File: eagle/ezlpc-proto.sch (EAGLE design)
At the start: 61 parts, among them J1 MICRO USB, Q1 12Mhz, T1 MMBT3906, U1 PRTR5V0U2X, U2 MIC5225-3.3v, U3 LPC11U35FHI33/501, U4 BAS40-05

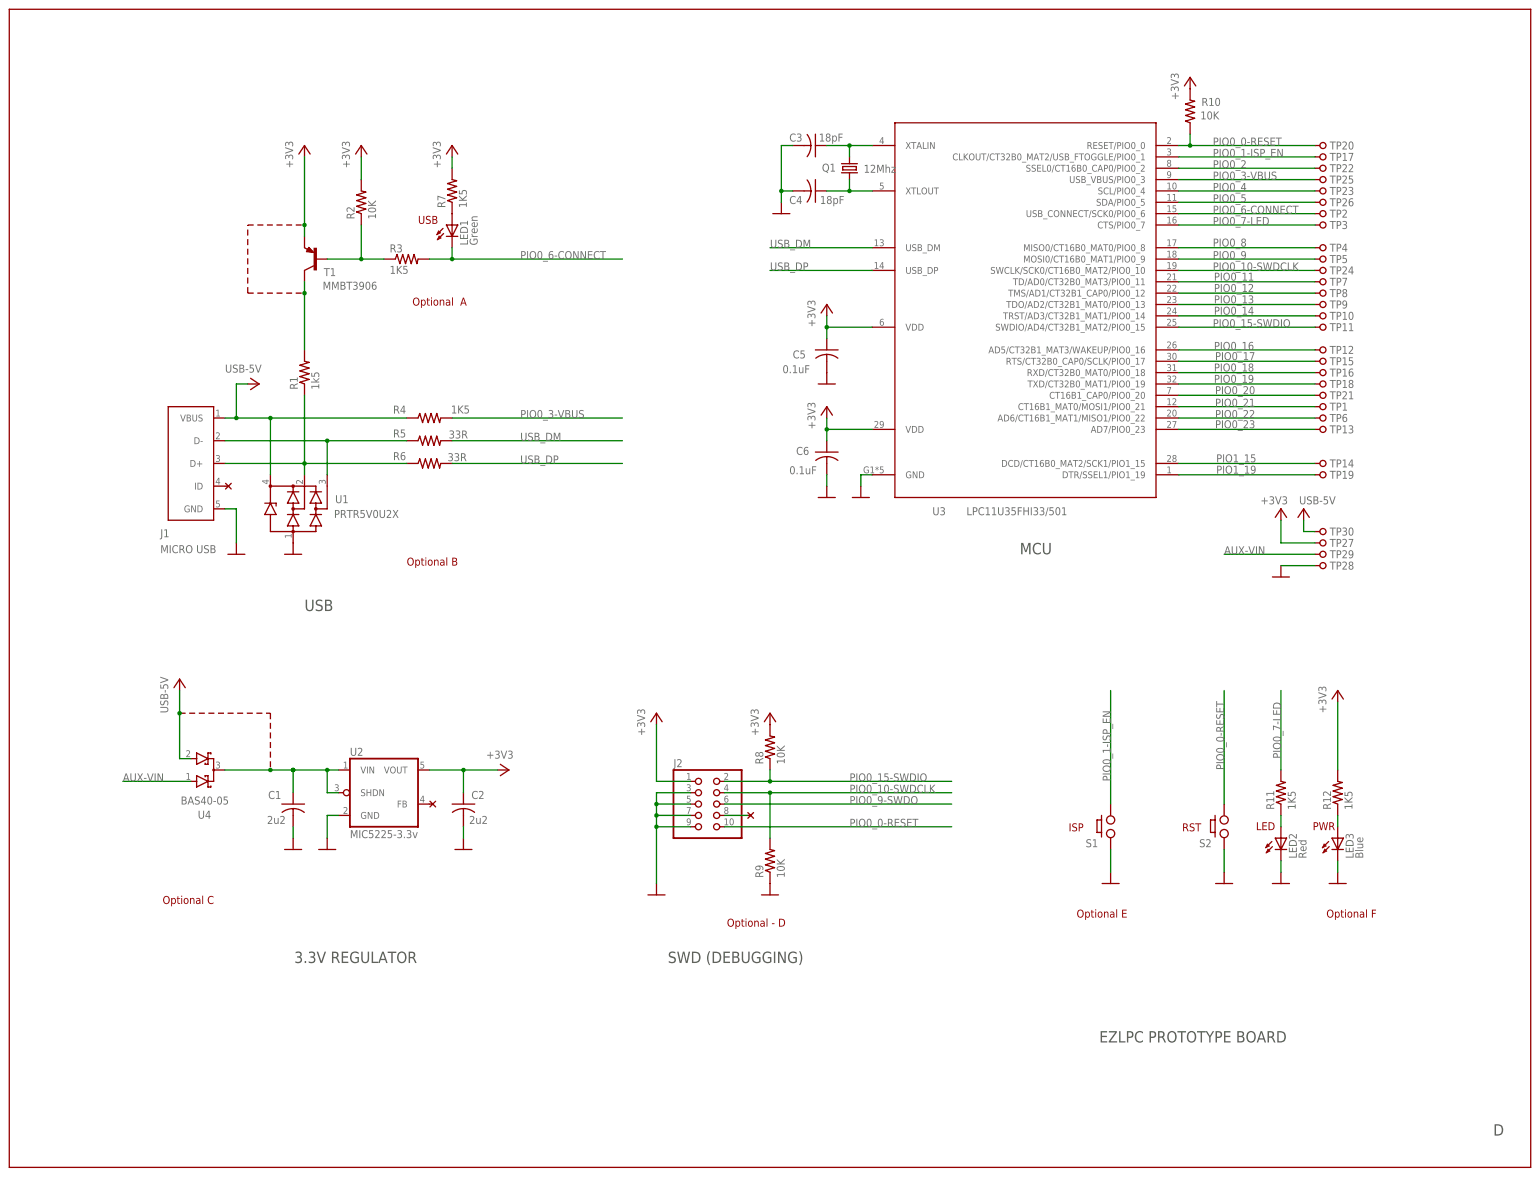
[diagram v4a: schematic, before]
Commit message: Cleaned up ERC warnings.
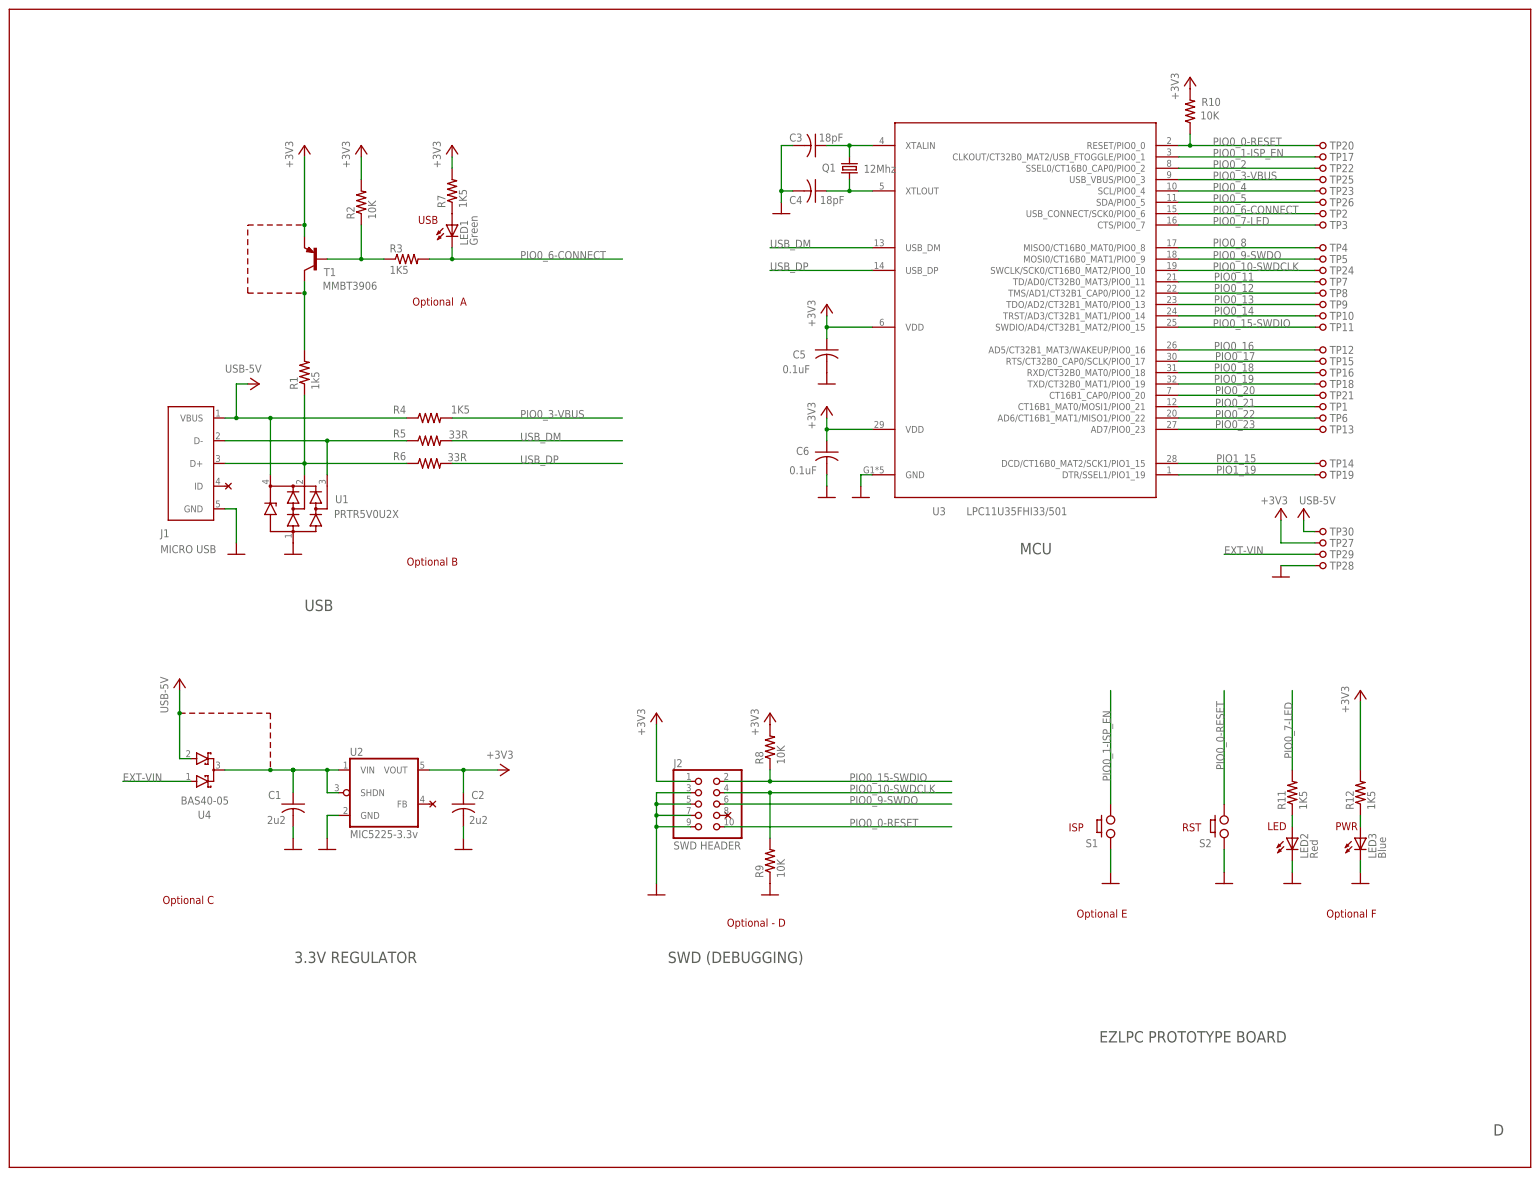
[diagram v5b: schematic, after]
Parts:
- J2: value (none) -> SWD HEADER
- TP1, TP10, TP11, TP12, TP13, TP14, TP15, TP16, TP17, TP18, TP19, TP2, TP20, TP21, TP22, TP23, TP24, TP25, TP26, TP27, TP28, TP29, TP3, TP30, TP4, TP5, TP6, TP7, TP8, TP9: value (none) -> HDR1
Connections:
- net AUX-VIN renamed EXT-VIN
- removed net N$11: J2.8
- removed net PIO0_9: TP5.1, U3.MOSI0/CT16B0_MAT1/PIO0_9
- net PIO0_9-SWDO: now also TP5.1, U3.MOSI0/CT16B0_MAT1/PIO0_9
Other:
- moved on the sheet: LED2, LED3, R11, R12

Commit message: Minor text changes.
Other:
- note added: "ARM MINI PRO"
- note added: "STUFF"
- note removed: "EZLPC PROTOTYPE BOARD"
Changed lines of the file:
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@@
 <sheet>
 <plain>
-<text x="243.84" y="27.94" size="2.54" layer="97" font="vector">EZLPC PROTOTYPE BOARD</text>
+<text x="243.84" y="27.94" size="2.54" layer="97" font="vector">ARM MINI PRO</text>
 <wire x1="0" y1="259.08" x2="340.36" y2="259.08" width="0.1524" layer="94"/>
 <wire x1="340.36" y1="259.08" x2="340.36" y2="0" width="0.1524" layer="94"/>
@@
 </polygon>
 <text x="66.04" y="124.46" size="2.54" layer="97">USB</text>
-<text x="147.32" y="45.72" size="2.54" layer="97">SWD (DEBUGGING)</text>
+<text x="144.78" y="45.72" size="2.54" layer="97">SWD (DEBUGGING)</text>
 <polygon width="0.1524" layer="98">
 <vertex x="17.78" y="96.52"/>
@@
 <text x="296.672" y="75.438" size="1.778" layer="94">PWR</text>
 <text x="91.44" y="211.074" size="1.778" layer="94">USB</text>
+<text x="251.46" y="45.72" size="2.54" layer="97">STUFF</text>
 </plain>
 <instances>
